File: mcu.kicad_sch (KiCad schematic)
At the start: 6 parts, among them U1 PIC32MX795F512L-80x-PF

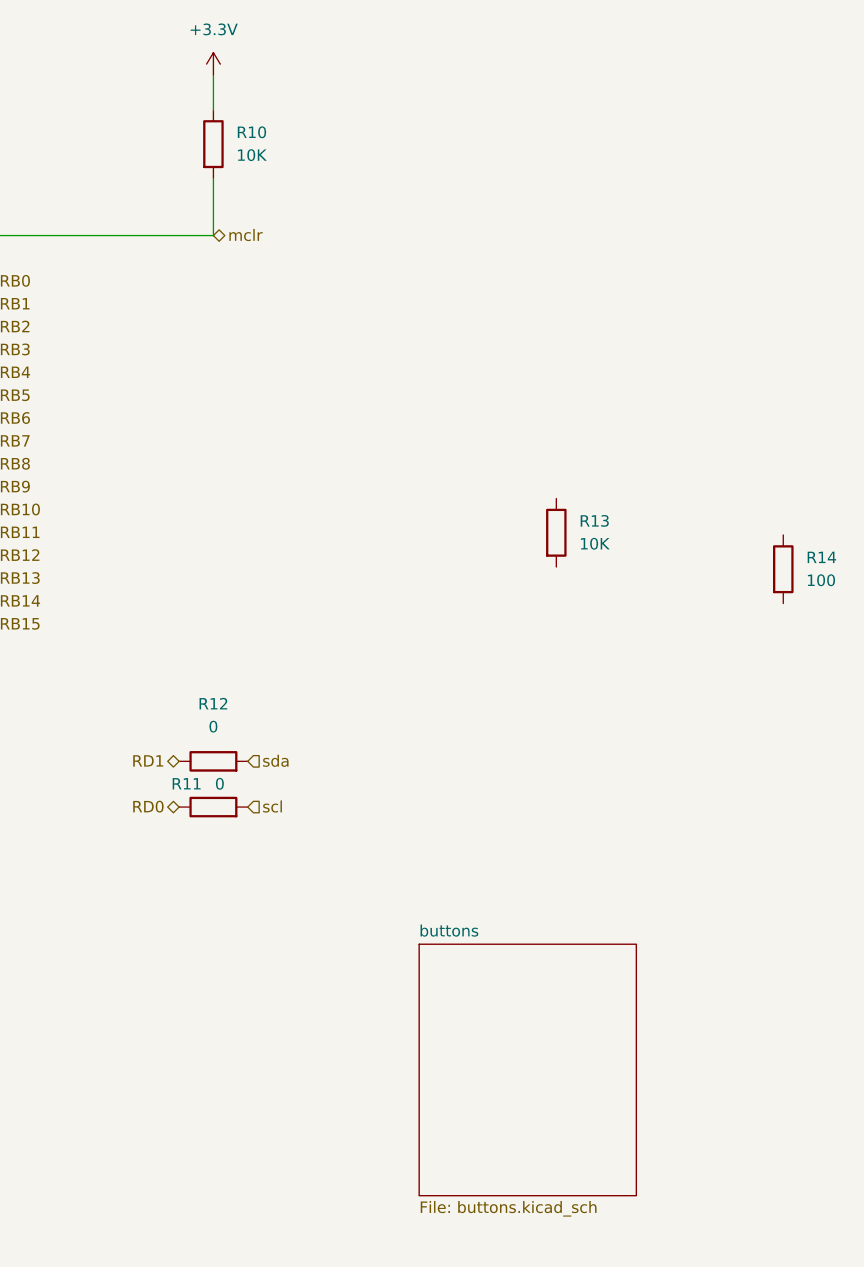
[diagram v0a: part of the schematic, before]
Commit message: feat: PCB layout updates, schematic changes, fp-lib-table config
- cnc_pic32.kicad_pcb: component repositioning, board outline, text formatting
- cnc_pic32.kicad_prl/pro: project settings updates
- fp-lib-table: add Library path to Library.pretty
- mcu.kicad_sch: PIC32 pin configuration updates
- zigbee.kicad_sch: MRF24J40 module updates
- oscilator.kicad_sch: crystal configuration
- power.kicad_sch/power_ft232.kicad_sch: power supply updates
- oled.kicad_sch: OLED display connections
- idc.kicad_sch: IDC connector updates
- osc_ft232.kicad_sch: FT232 crystal
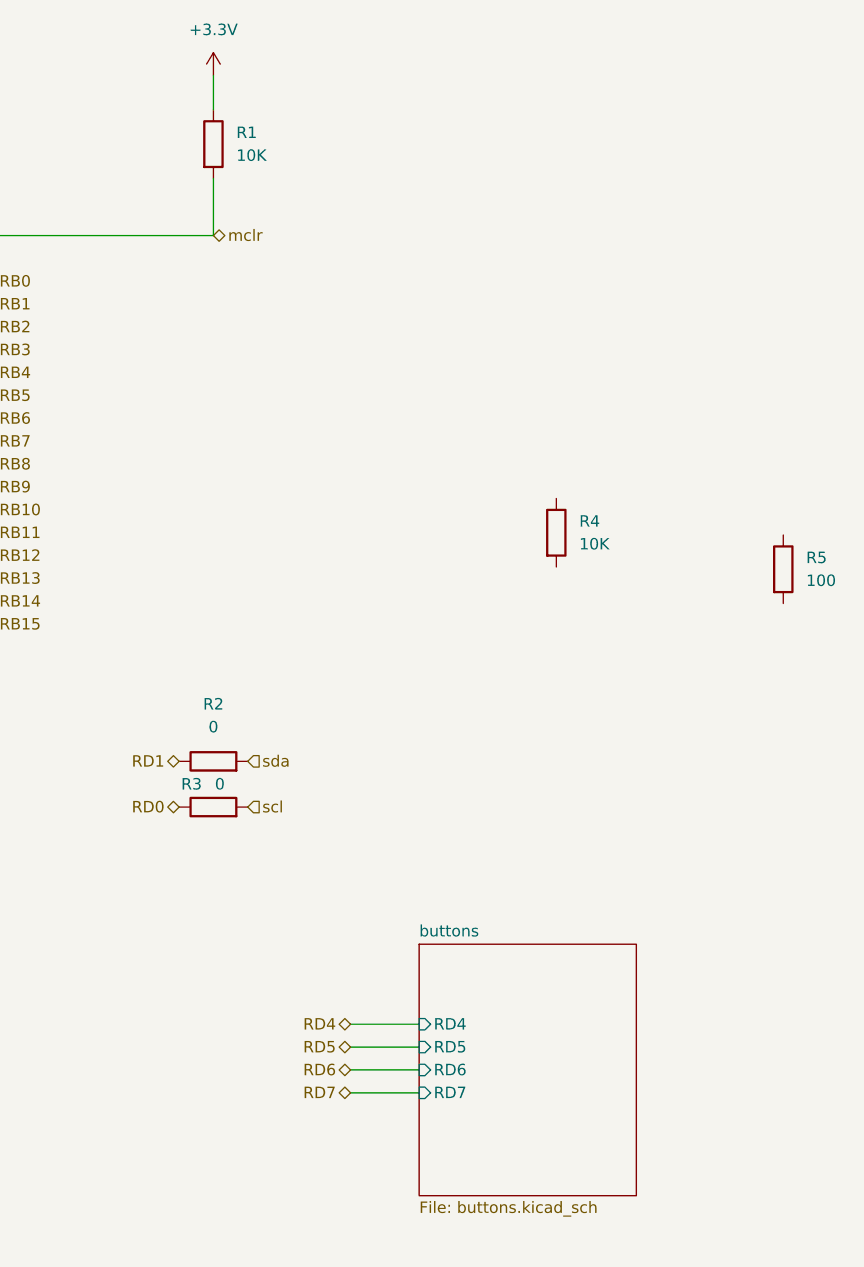
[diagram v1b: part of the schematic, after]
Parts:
- renumbered R10 to R1, R12 to R2, R11 to R3, R13 to R4, R14 to R5
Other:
- sheet buttons ports: added RD4, RD5, RD6, RD7; removed none
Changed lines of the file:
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@@
+	(wire
+		(pts
+			(xy 218.44 130.81) (xy 226.06 130.81)
+		)
+		(stroke
+			(width 0)
+			(type default)
+		)
+	)
 	(wire
 		(pts
@@
 	(wire
 		(pts
+			(xy 218.44 128.27) (xy 226.06 128.27)
+		)
+		(stroke
+			(width 0)
+			(type default)
+		)
+	)
+	(wire
+		(pts
 			(xy 129.54 27.94) (xy 132.08 27.94)
 		)
@@
 	(wire
 		(pts
+			(xy 218.44 133.35) (xy 226.06 133.35)
+		)
+		(stroke
+			(width 0)
+			(type default)
+		)
+	)
+	(wire
+		(pts
 			(xy 165.1 66.04) (xy 177.8 66.04)
 		)
@@
 		(pts
 			(xy 127 27.94) (xy 129.54 27.94)
+		)
+		(stroke
+			(width 0)
+			(type default)
+		)
+	)
+	(wire
+		(pts
+			(xy 218.44 125.73) (xy 226.06 125.73)
 		)
 		(stroke
@@
 		)
 	)
+	(hierarchical_label "RD7"
+		(shape bidirectional)
+		(at 218.44 133.35 180)
+		(effects
+			(font
+				(size 1.27 1.27)
+			)
+			(justify right)
+		)
+	)
 	(hierarchical_label "OSC2"
 		(shape input)
@@
 		)
 	)
+	(hierarchical_label "RD5"
+		(shape bidirectional)
+		(at 218.44 128.27 180)
+		(effects
+			(font
+				(size 1.27 1.27)
+			)
+			(justify right)
+		)
+	)
 	(hierarchical_label "RD0"
 		(shape bidirectional)
@@
 		)
 	)
+	(hierarchical_label "RD4"
+		(shape bidirectional)
+		(at 218.44 125.73 180)
+		(effects
+			(font
+				(size 1.27 1.27)
+			)
+			(justify right)
+		)
+	)
 	(hierarchical_label "RA15"
 		(shape bidirectional)
@@
 		(shape bidirectional)
 		(at 104.14 114.3 180)
+		(effects
+			(font
+				(size 1.27 1.27)
+			)
+			(justify right)
+		)
+	)
+	(hierarchical_label "RD6"
+		(shape bidirectional)
+		(at 218.44 130.81 180)
 		(effects
 			(font
@@
 		(in_pos_files yes)
 		(dnp no)
-		(property "Reference" "R11"
+		(property "Reference" "R3"
 			(at 201.93 99.06 90)
 			(show_name no)
@@
 			(project "cnc_pic32"
 				(path "/13dbfc1f-be47-44ca-9042-3d6a9a657d7d/64cf98d4-7353-423c-baad-4e05534717be"
-					(reference "R11")
+					(reference "R3")
 					(unit 1)
 				)
@@
 		(dnp no)
 		(fields_autoplaced yes)
-		(property "Reference" "R14"
+		(property "Reference" "R5"
 			(at 269.057 73.905 0)
 			(show_name no)
@@
 			(project "cnc_pic32"
 				(path "/13dbfc1f-be47-44ca-9042-3d6a9a657d7d/64cf98d4-7353-423c-baad-4e05534717be"
-					(reference "R14")
+					(reference "R5")
 					(unit 1)
 				)
@@
 		(dnp no)
 		(fields_autoplaced yes)
-		(property "Reference" "R12"
+		(property "Reference" "R2"
 			(at 203.2 90.17 90)
 			(show_name no)
@@
 			(project "cnc_pic32"
 				(path "/13dbfc1f-be47-44ca-9042-3d6a9a657d7d/64cf98d4-7353-423c-baad-4e05534717be"
-					(reference "R12")
+					(reference "R2")
 					(unit 1)
 				)
@@
 		(dnp no)
 		(fields_autoplaced yes)
-		(property "Reference" "R13"
+		(property "Reference" "R4"
 			(at 243.84 69.85 0)
 			(show_name no)
@@
 			(project "cnc_pic32"
 				(path "/13dbfc1f-be47-44ca-9042-3d6a9a657d7d/64cf98d4-7353-423c-baad-4e05534717be"
-					(reference "R13")
+					(reference "R4")
 					(unit 1)
 				)
@@
 		(dnp no)
 		(fields_autoplaced yes)
-		(property "Reference" "R10"
+		(property "Reference" "R1"
 			(at 205.74 26.67 0)
 			(show_name no)
@@
 			(project "cnc_pic32"
 				(path "/13dbfc1f-be47-44ca-9042-3d6a9a657d7d/64cf98d4-7353-423c-baad-4e05534717be"
-					(reference "R10")
+					(reference "R1")
 					(unit 1)
 				)
@@
 			)
 		)
+		(pin "RD6" input
+			(at 226.06 130.81 180)
+			(effects
+				(font
+					(size 1.27 1.27)
+				)
+				(justify left)
+			)
+		)
+		(pin "RD7" input
+			(at 226.06 133.35 180)
+			(effects
+				(font
+					(size 1.27 1.27)
+				)
+				(justify left)
+			)
+		)
+		(pin "RD4" input
+			(at 226.06 125.73 180)
+			(effects
+				(font
+					(size 1.27 1.27)
+				)
+				(justify left)
+			)
+		)
+		(pin "RD5" input
+			(at 226.06 128.27 180)
+			(effects
+				(font
+					(size 1.27 1.27)
+				)
+				(justify left)
+			)
+		)

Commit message: fix: unify +3.3V to +3V3 across all schematics and PCB
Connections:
- net +3.3V: no longer names the net of U1.16 (VDD), U1.2 (VDD), U1.30 (AVDD), U1.37 (VDD), U1.46 (VDD), U1.55 (VUSB3V3), U1.62 (VDD), U1.85 (VCAP/VDDCORE), U1.86 (VDD)
- net +3.3V: no longer R1.1
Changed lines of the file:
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@@
 	)
 	(symbol
-		(lib_id "power:+3.3V")
+		(lib_id "power:+3V3")
 		(at 121.92 21.59 0)
 		(unit 1)
@@
 			)
 		)
-		(property "Value" "+3.3V"
+		(property "Value" "+3V3"
 			(at 121.92 16.51 0)
 			(show_name no)
@@
 	)
 	(symbol
-		(lib_id "power:+3.3V")
+		(lib_id "power:+3V3")
 		(at 203.2 20.32 0)
 		(unit 1)
@@
 			)
 		)
-		(property "Value" "+3.3V"
+		(property "Value" "+3V3"
 			(at 203.2 15.24 0)
 			(show_name no)

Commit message: feat: integrate zigbee sheet + R 0603→0805 footprint update
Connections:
- net +3.3V: now reaches U1.16 (VDD), U1.2 (VDD), U1.30 (AVDD), U1.37 (VDD), U1.46 (VDD), U1.55 (VUSB3V3), U1.62 (VDD), U1.85 (VCAP/VDDCORE), U1.86 (VDD)
- net +3.3V: now also R1.1
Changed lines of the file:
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@@
-	)
-	(symbol
-		(lib_id "power:+3V3")
-		(at 121.92 21.59 0)
-		(unit 1)
-		(body_style 1)
-		(exclude_from_sim no)
-		(in_bom yes)
-		(on_board yes)
-		(in_pos_files yes)
-		(dnp no)
-		(fields_autoplaced yes)
-		(property "Reference" "#PWR01"
-			(at 121.92 25.4 0)
-			(hide yes)
-			(show_name no)
-			(do_not_autoplace no)
-			(effects
-				(font
-					(size 1.27 1.27)
-				)
-			)
-		)
-		(property "Value" "+3V3"
-			(at 121.92 16.51 0)
-			(show_name no)
-			(do_not_autoplace no)
-			(effects
-				(font
-					(size 1.27 1.27)
-				)
-			)
-		)
-		(property "Footprint" ""
-			(at 121.92 21.59 0)
-			(hide yes)
-			(show_name no)
-			(do_not_autoplace no)
-			(effects
-				(font
-					(size 1.27 1.27)
-				)
-			)
-		)
-		(property "Datasheet" ""
-			(at 121.92 21.59 0)
-			(hide yes)
-			(show_name no)
-			(do_not_autoplace no)
-			(effects
-				(font
-					(size 1.27 1.27)
-				)
-			)
-		)
-		(property "Description" "Power symbol creates a global label with name \"+3.3V\""
-			(at 121.92 21.59 0)
-			(hide yes)
-			(show_name no)
-			(do_not_autoplace no)
-			(effects
-				(font
-					(size 1.27 1.27)
-				)
-			)
-		)
-		(pin "1"
-		)
-		(instances
-			(project "cnc_pic32"
-				(path "/13dbfc1f-be47-44ca-9042-3d6a9a657d7d/64cf98d4-7353-423c-baad-4e05534717be"
-					(reference "#PWR01")
-					(unit 1)
-				)
-			)
-		)
 	)
 	(symbol
@@
 	)
 	(symbol
-		(lib_id "power:+3V3")
-		(at 203.2 20.32 0)
-		(unit 1)
-		(body_style 1)
-		(exclude_from_sim no)
-		(in_bom yes)
-		(on_board yes)
-		(in_pos_files yes)
-		(dnp no)
-		(fields_autoplaced yes)
-		(property "Reference" "#PWR03"
-			(at 203.2 24.13 0)
-			(hide yes)
-			(show_name no)
-			(do_not_autoplace no)
-			(effects
-				(font
-					(size 1.27 1.27)
-				)
-			)
-		)
-		(property "Value" "+3V3"
-			(at 203.2 15.24 0)
-			(show_name no)
-			(do_not_autoplace no)
-			(effects
-				(font
-					(size 1.27 1.27)
-				)
-			)
-		)
-		(property "Footprint" ""
-			(at 203.2 20.32 0)
-			(hide yes)
-			(show_name no)
-			(do_not_autoplace no)
-			(effects
-				(font
-					(size 1.27 1.27)
-				)
-			)
-		)
-		(property "Datasheet" ""
-			(at 203.2 20.32 0)
-			(hide yes)
-			(show_name no)
-			(do_not_autoplace no)
-			(effects
-				(font
-					(size 1.27 1.27)
-				)
-			)
-		)
-		(property "Description" "Power symbol creates a global label with name \"+3.3V\""
-			(at 203.2 20.32 0)
-			(hide yes)
-			(show_name no)
-			(do_not_autoplace no)
-			(effects
-				(font
-					(size 1.27 1.27)
-				)
-			)
-		)
-		(pin "1"
-		)
-		(instances
-			(project "cnc_pic32"
-				(path "/13dbfc1f-be47-44ca-9042-3d6a9a657d7d/64cf98d4-7353-423c-baad-4e05534717be"
-					(reference "#PWR03")
-					(unit 1)
-				)
-			)
-		)
-	)
-	(symbol
 		(lib_id "Device:R")
 		(at 241.3 71.12 0)
@@
 				(path "/13dbfc1f-be47-44ca-9042-3d6a9a657d7d/64cf98d4-7353-423c-baad-4e05534717be"
 					(reference "R4")
+					(unit 1)
+				)
+			)
+		)
+	)
+	(symbol
+		(lib_id "power:+3.3V")
+		(at 203.2 20.32 0)
+		(unit 1)
+		(body_style 1)
+		(exclude_from_sim no)
+		(in_bom yes)
+		(on_board yes)
+		(in_pos_files yes)
+		(dnp no)
+		(fields_autoplaced yes)
+		(property "Reference" "#PWR03"
+			(at 203.2 24.13 0)
+			(hide yes)
+			(show_name no)
+			(do_not_autoplace no)
+			(effects
+				(font
+					(size 1.27 1.27)
+				)
+			)
+		)
+		(property "Value" "+3.3V"
+			(at 203.2 15.24 0)
+			(show_name no)
+			(do_not_autoplace no)
+			(effects
+				(font
+					(size 1.27 1.27)
+				)
+			)
+		)
+		(property "Footprint" ""
+			(at 203.2 20.32 0)
+			(hide yes)
+			(show_name no)
+			(do_not_autoplace no)
+			(effects
+				(font
+					(size 1.27 1.27)
+				)
+			)
+		)
+		(property "Datasheet" ""
+			(at 203.2 20.32 0)
+			(hide yes)
+			(show_name no)
+			(do_not_autoplace no)
+			(effects
+				(font
+					(size 1.27 1.27)
+				)
+			)
+		)
+		(property "Description" ""
+			(at 203.2 20.32 0)
+			(show_name no)
+			(do_not_autoplace no)
+			(effects
+				(font
+					(size 1.27 1.27)
+				)
+			)
+		)
+		(pin "1"
+		)
+		(instances
+			(project "cnc_pic32"
+				(path "/13dbfc1f-be47-44ca-9042-3d6a9a657d7d/64cf98d4-7353-423c-baad-4e05534717be"
+					(reference "#PWR03")
 					(unit 1)
 				)
@@
 					(unit 1)
 				)
+			)
+		)
+	)
+	(symbol
+		(lib_id "power:+3.3V")
+		(at 121.92 21.59 0)
+		(unit 1)
+		(body_style 1)
+		(exclude_from_sim no)
+		(in_bom yes)
+		(on_board yes)
+		(in_pos_files yes)
+		(dnp no)
+		(fields_autoplaced yes)
+		(property "Reference" "#PWR01"
+			(at 121.92 25.4 0)
+			(hide yes)
+			(show_name no)
+			(do_not_autoplace no)
+			(effects
+				(font
+					(size 1.27 1.27)
+				)
+			)
+		)
+		(property "Value" "+3.3V"
+			(at 121.92 16.51 0)
+			(show_name no)
+			(do_not_autoplace no)
+			(effects
+				(font
+					(size 1.27 1.27)
+				)
+			)
+		)
+		(property "Footprint" ""
+			(at 121.92 21.59 0)
+			(hide yes)
+			(show_name no)
+			(do_not_autoplace no)
+			(effects
+				(font
+					(size 1.27 1.27)
+				)
+			)
+		)
+		(property "Datasheet" ""
+			(at 121.92 21.59 0)
+			(hide yes)
+			(show_name no)
+			(do_not_autoplace no)
+			(effects
+				(font
+					(size 1.27 1.27)
+				)
+			)
+		)
+		(property "Description" ""
+			(at 121.92 21.59 0)
+			(show_name no)
+			(do_not_autoplace no)
+			(effects
+				(font
+					(size 1.27 1.27)
+				)
+			)
+		)
+		(pin "1"
+		)
+		(instances
+			(project "cnc_pic32"
+				(path "/13dbfc1f-be47-44ca-9042-3d6a9a657d7d/64cf98d4-7353-423c-baad-4e05534717be"
+					(reference "#PWR01")
+					(unit 1)
+				)
